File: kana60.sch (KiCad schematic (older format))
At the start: 2 parts

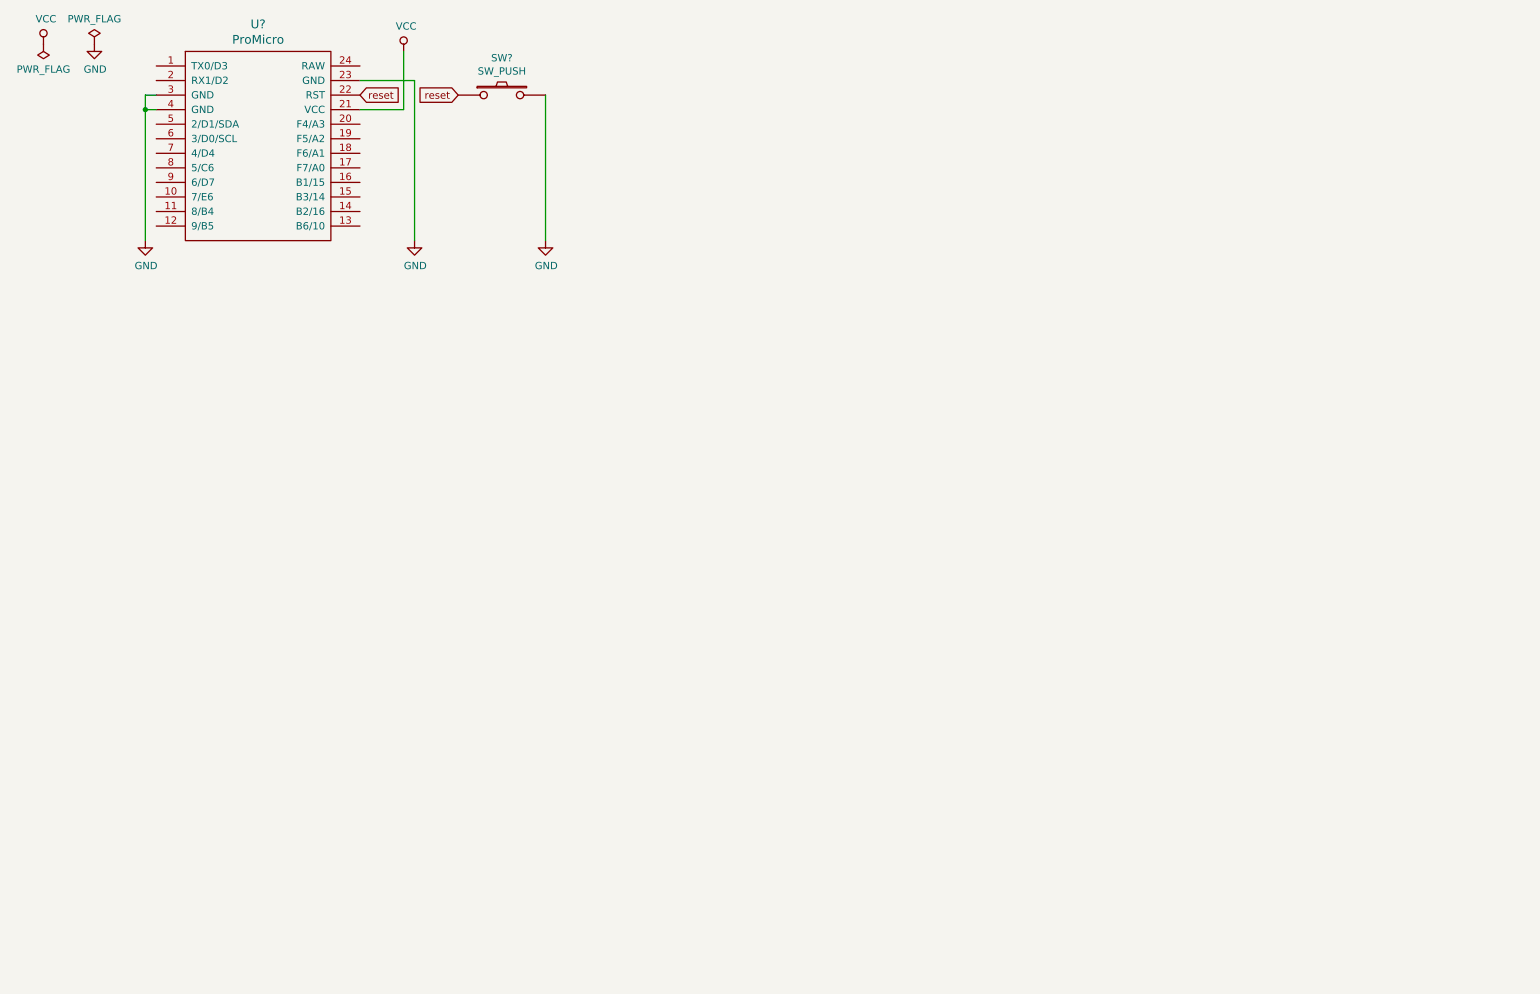
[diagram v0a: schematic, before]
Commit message: add key switches
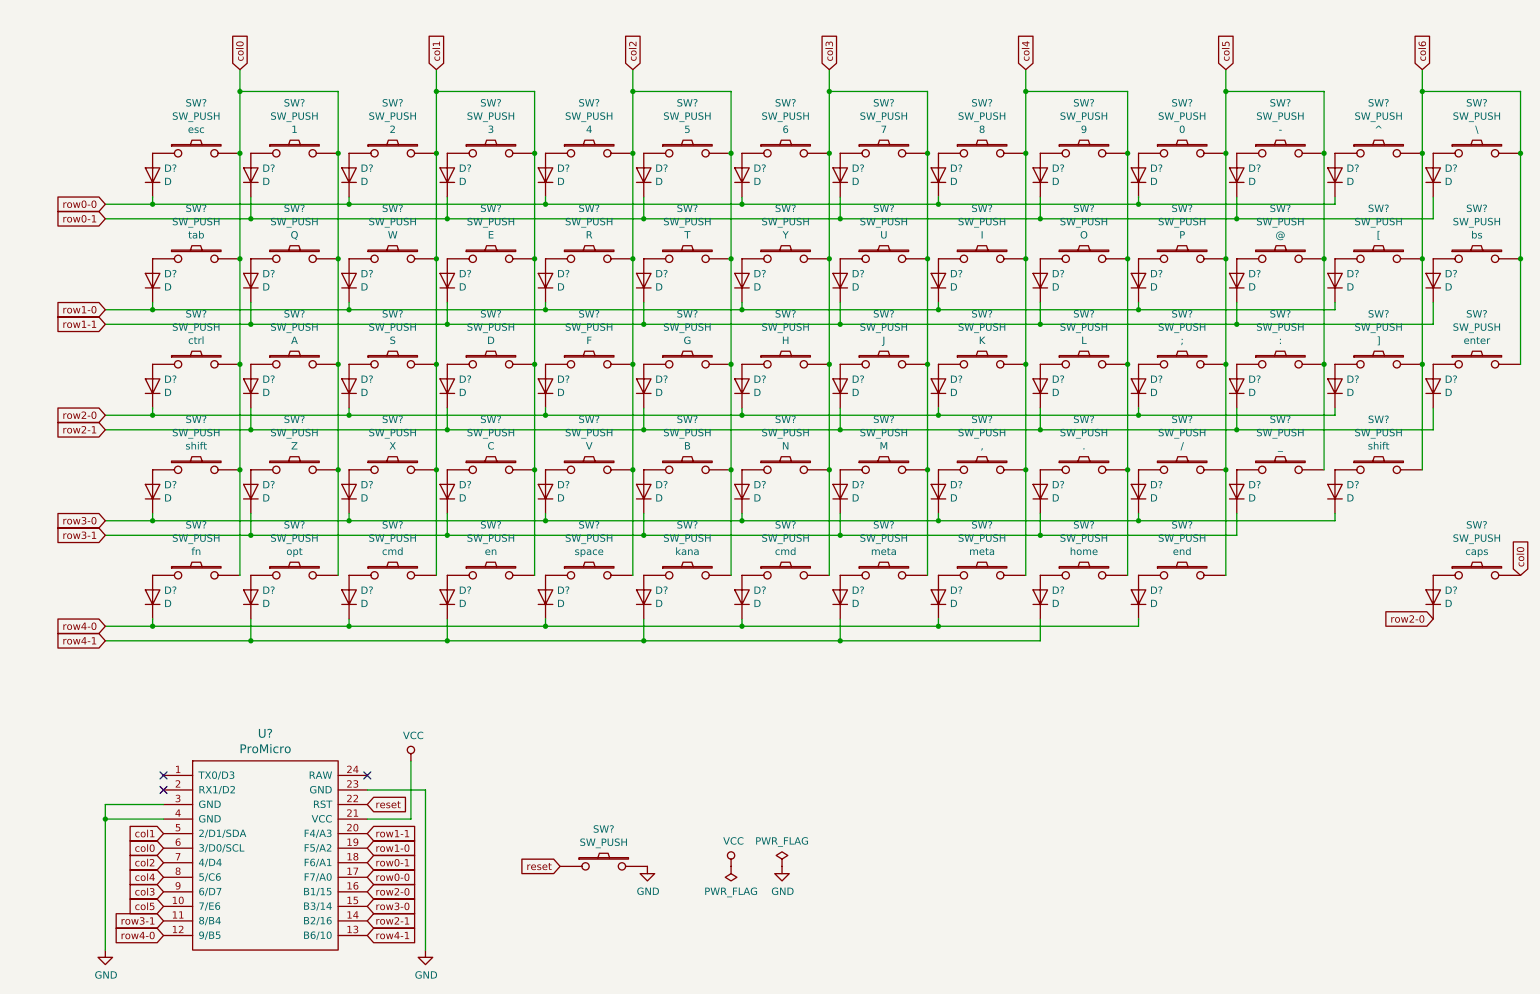
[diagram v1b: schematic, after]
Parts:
- added D? (x67): D, symbol Device:D
- added SW?: SW_PUSH, esc, symbol kbd:SW_PUSH
- added SW?: SW_PUSH, tab, symbol kbd:SW_PUSH
- added SW?: SW_PUSH, 1, symbol kbd:SW_PUSH
- added SW?: SW_PUSH, Q, symbol kbd:SW_PUSH
- added SW?: SW_PUSH, ctrl, symbol kbd:SW_PUSH
- added SW? (x2): SW_PUSH, shift, symbol kbd:SW_PUSH
- added SW?: SW_PUSH, A, symbol kbd:SW_PUSH
- added SW?: SW_PUSH, Z, symbol kbd:SW_PUSH
- added SW?: SW_PUSH, fn, symbol kbd:SW_PUSH
- added SW?: SW_PUSH, opt, symbol kbd:SW_PUSH
- added SW?: SW_PUSH, 2, symbol kbd:SW_PUSH
- added SW?: SW_PUSH, W, symbol kbd:SW_PUSH
- added SW?: SW_PUSH, 3, symbol kbd:SW_PUSH
- added SW?: SW_PUSH, E, symbol kbd:SW_PUSH
- added SW?: SW_PUSH, S, symbol kbd:SW_PUSH
- added SW?: SW_PUSH, X, symbol kbd:SW_PUSH
- added SW?: SW_PUSH, D, symbol kbd:SW_PUSH
- added SW?: SW_PUSH, C, symbol kbd:SW_PUSH
- added SW? (x2): SW_PUSH, cmd, symbol kbd:SW_PUSH
- added SW?: SW_PUSH, en, symbol kbd:SW_PUSH
- added SW?: SW_PUSH, 4, symbol kbd:SW_PUSH
- added SW?: SW_PUSH, R, symbol kbd:SW_PUSH
- added SW?: SW_PUSH, 5, symbol kbd:SW_PUSH
- added SW?: SW_PUSH, T, symbol kbd:SW_PUSH
- added SW?: SW_PUSH, F, symbol kbd:SW_PUSH
- added SW?: SW_PUSH, V, symbol kbd:SW_PUSH
- added SW?: SW_PUSH, G, symbol kbd:SW_PUSH
- added SW?: SW_PUSH, B, symbol kbd:SW_PUSH
- added SW?: SW_PUSH, space, symbol kbd:SW_PUSH
- added SW?: SW_PUSH, 6, symbol kbd:SW_PUSH
- added SW?: SW_PUSH, Y, symbol kbd:SW_PUSH
- added SW?: SW_PUSH, 7, symbol kbd:SW_PUSH
- added SW?: SW_PUSH, H, symbol kbd:SW_PUSH
- added SW?: SW_PUSH, N, symbol kbd:SW_PUSH
- added SW?: SW_PUSH, 8, symbol kbd:SW_PUSH
- added SW?: SW_PUSH, U, symbol kbd:SW_PUSH
- added SW?: SW_PUSH, 9, symbol kbd:SW_PUSH
- added SW?: SW_PUSH, I, symbol kbd:SW_PUSH
- added SW?: SW_PUSH, J, symbol kbd:SW_PUSH
- added SW?: SW_PUSH, M, symbol kbd:SW_PUSH
- added SW?: SW_PUSH, K, symbol kbd:SW_PUSH
- added SW?: SW_PUSH, ,, symbol kbd:SW_PUSH
- added SW?: SW_PUSH, kana, symbol kbd:SW_PUSH
- added SW?: SW_PUSH, 0, symbol kbd:SW_PUSH
- added SW?: SW_PUSH, O, symbol kbd:SW_PUSH
- added SW?: SW_PUSH, -, symbol kbd:SW_PUSH
- added SW?: SW_PUSH, P, symbol kbd:SW_PUSH
- added SW?: SW_PUSH, L, symbol kbd:SW_PUSH
- added SW?: SW_PUSH, ., symbol kbd:SW_PUSH
- added SW?: SW_PUSH, ;, symbol kbd:SW_PUSH
- added SW?: SW_PUSH, /, symbol kbd:SW_PUSH
- added SW? (x2): SW_PUSH, meta, symbol kbd:SW_PUSH
- added SW?: SW_PUSH, ^, symbol kbd:SW_PUSH
- added SW?: SW_PUSH, @, symbol kbd:SW_PUSH
- added SW?: SW_PUSH, \\, symbol kbd:SW_PUSH
- added SW?: SW_PUSH, [, symbol kbd:SW_PUSH
- added SW?: SW_PUSH, :, symbol kbd:SW_PUSH
- added SW?: SW_PUSH, _, symbol kbd:SW_PUSH
- added SW?: SW_PUSH, ], symbol kbd:SW_PUSH
- added SW?: SW_PUSH, home, symbol kbd:SW_PUSH
- added SW?: SW_PUSH, end, symbol kbd:SW_PUSH
- added SW?: SW_PUSH, bs, symbol kbd:SW_PUSH
- added SW?: SW_PUSH, enter, symbol kbd:SW_PUSH
- added SW?: SW_PUSH, caps, symbol kbd:SW_PUSH
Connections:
- net col5: now reaches U?.10 (7/E6)
- net col5: now also SW?.2, SW?.2, SW?.2, SW?.2, SW?.2, SW?.2, SW?.2, SW?.2, SW?.2
- net row3-1: now reaches U?.11 (8/B4)
- net row3-1: now also D?.1 (K), D?.1 (K), D?.1 (K), D?.1 (K), D?.1 (K), D?.1 (K)
- net row4-0: now reaches U?.12 (9/B5)
- net row4-0: now also D?.1 (K), D?.1 (K), D?.1 (K), D?.1 (K), D?.1 (K), D?.1 (K)
- net row4-1: now reaches U?.13 (B6/10)
- net row4-1: now also D?.1 (K), D?.1 (K), D?.1 (K), D?.1 (K), D?.1 (K)
- net row2-1: now reaches U?.14 (B2/16)
- net row2-1: now also D?.1 (K), D?.1 (K), D?.1 (K), D?.1 (K), D?.1 (K), D?.1 (K), D?.1 (K)
- net row3-0: now reaches U?.15 (B3/14)
- net row3-0: now also D?.1 (K), D?.1 (K), D?.1 (K), D?.1 (K), D?.1 (K), D?.1 (K), D?.1 (K)
- net row2-0: now reaches U?.16 (B1/15)
- net row2-0: now also D?.1 (K), D?.1 (K), D?.1 (K), D?.1 (K), D?.1 (K), D?.1 (K), D?.1 (K), D?.1 (K)
- net row0-0: now reaches U?.17 (F7/A0)
- net row0-0: now also D?.1 (K), D?.1 (K), D?.1 (K), D?.1 (K), D?.1 (K), D?.1 (K), D?.1 (K)
- net row0-1: now reaches U?.18 (F6/A1)
- net row0-1: now also D?.1 (K), D?.1 (K), D?.1 (K), D?.1 (K), D?.1 (K), D?.1 (K), D?.1 (K)
- net row1-0: now reaches U?.19 (F5/A2)
- net row1-0: now also D?.1 (K), D?.1 (K), D?.1 (K), D?.1 (K), D?.1 (K), D?.1 (K), D?.1 (K)
- net row1-1: now reaches U?.20 (F4/A3)
- net row1-1: now also D?.1 (K), D?.1 (K), D?.1 (K), D?.1 (K), D?.1 (K), D?.1 (K), D?.1 (K)
- net col1: now reaches U?.5 (2/D1/SDA)
- net col1: now also SW?.2, SW?.2, SW?.2, SW?.2, SW?.2, SW?.2, SW?.2, SW?.2, SW?.2, SW?.2
- net col0: now reaches U?.6 (3/D0/SCL)
- net col0: now also SW?.2, SW?.2, SW?.2, SW?.2, SW?.2, SW?.2, SW?.2, SW?.2, SW?.2, SW?.2, SW?.2
- net col2: now reaches U?.7 (4/D4)
- net col2: now also SW?.2, SW?.2, SW?.2, SW?.2, SW?.2, SW?.2, SW?.2, SW?.2, SW?.2, SW?.2
- net col4: now reaches U?.8 (5/C6)
- net col4: now also SW?.2, SW?.2, SW?.2, SW?.2, SW?.2, SW?.2, SW?.2, SW?.2, SW?.2, SW?.2
- net col3: now reaches U?.9 (6/D7)
- net col3: now also SW?.2, SW?.2, SW?.2, SW?.2, SW?.2, SW?.2, SW?.2, SW?.2, SW?.2, SW?.2
- new net: D?.2 (A), SW?.1 (x67)
- new net col6: SW?.2, SW?.2, SW?.2, SW?.2, SW?.2, SW?.2, SW?.2
- no-connect marks 0 -> 3
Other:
- moved on the sheet: SW?, U?

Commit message: annotation and rule check
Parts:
- gave numbers to parts that had none: 136
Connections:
- net col2: now also U1.2 (RX1/D2); no longer U1.7 (4/D4)
- net col3: now also U1.7 (4/D4); no longer U1.9 (6/D7)
- net col4: now also U1.9 (6/D7); no longer U1.8 (5/C6)
- net col5: now also U1.8 (5/C6); no longer U1.10 (7/E6)
- net col6: now also U1.10 (7/E6)
- no-connect marks 3 -> 2

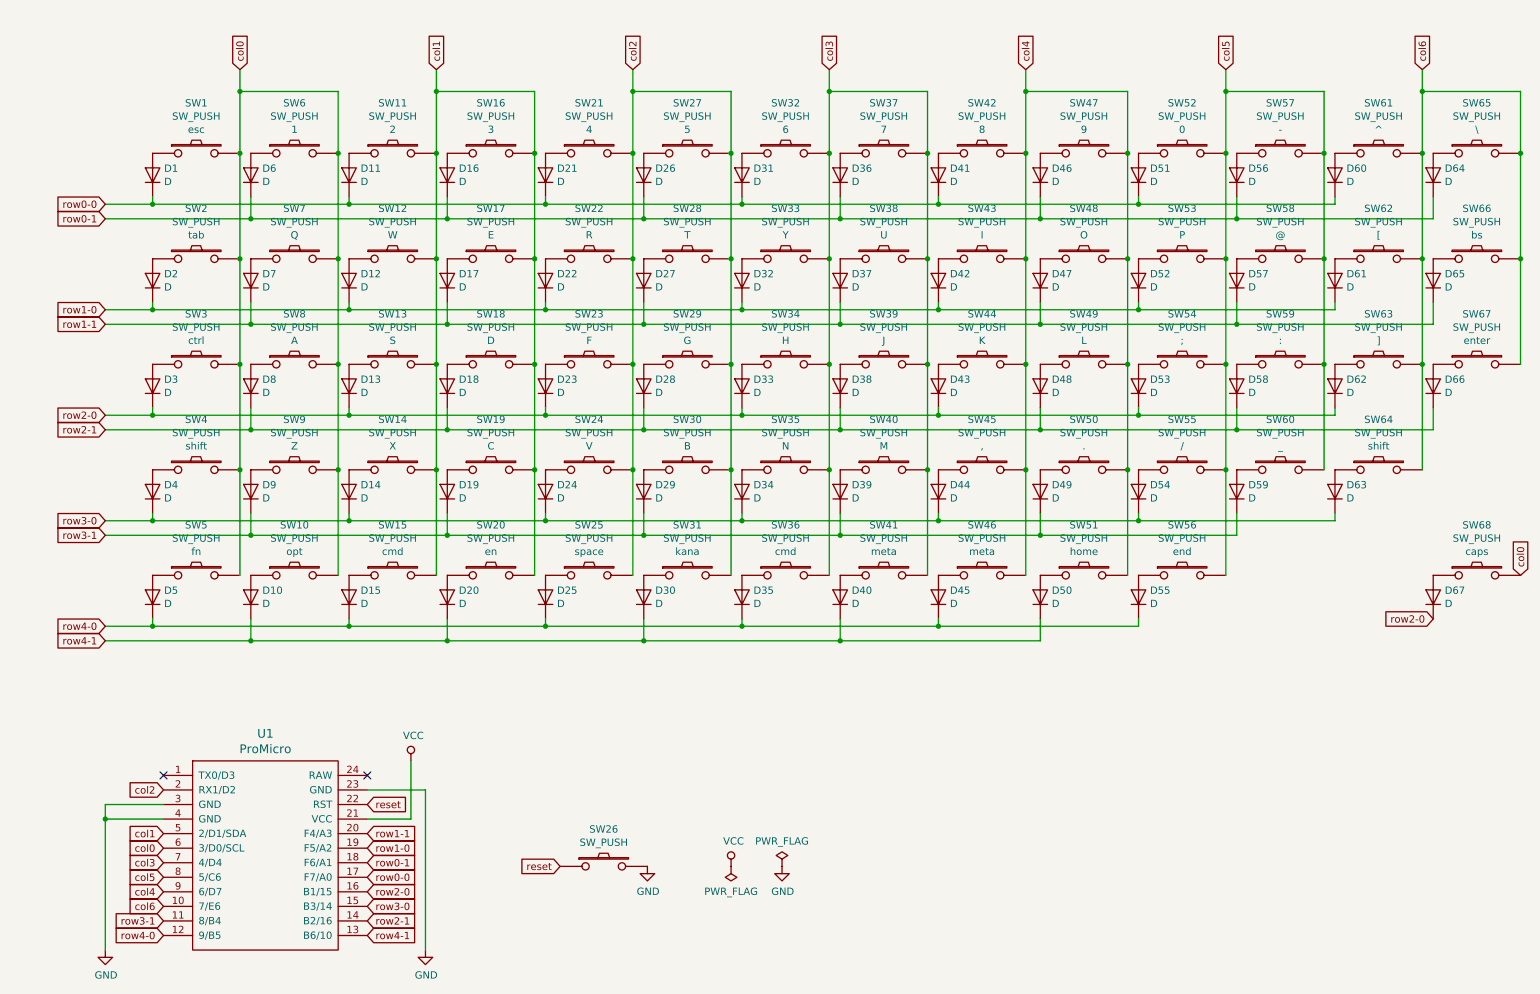
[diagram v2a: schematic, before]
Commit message: fix footprint
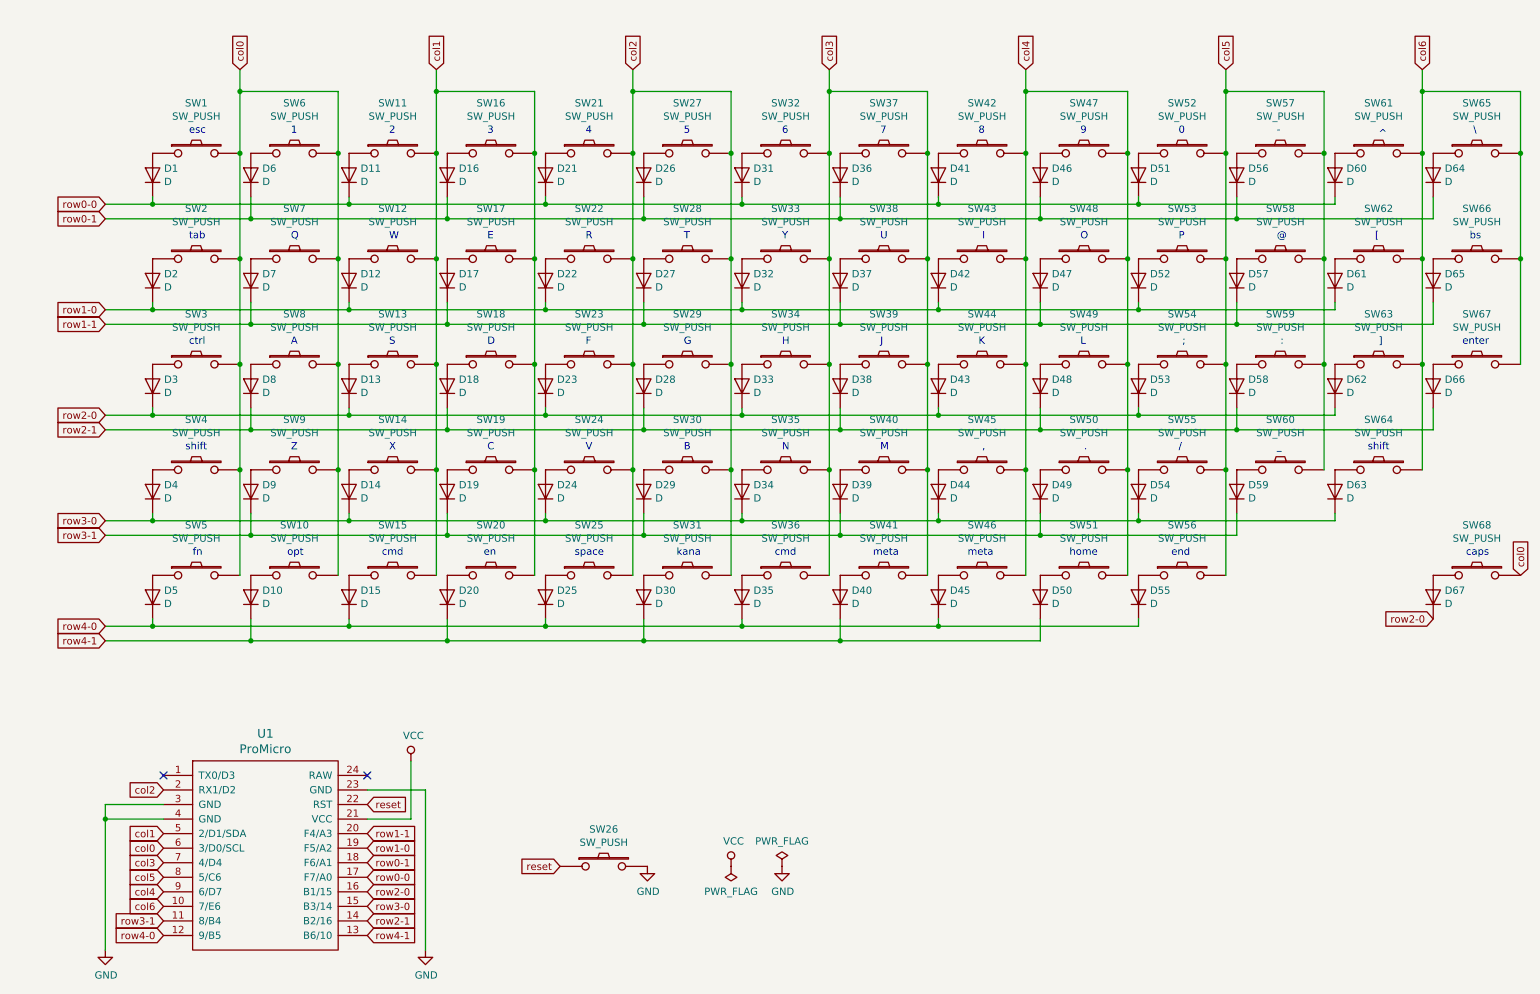
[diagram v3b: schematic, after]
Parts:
- SW1: footprint esc -> (none)
- SW10: footprint opt -> (none)
- SW11: footprint 2 -> (none)
- SW12: footprint W -> (none)
- SW13: footprint S -> (none)
- SW14: footprint X -> (none)
- SW15, SW36: footprint cmd -> (none)
- SW16: footprint 3 -> (none)
- SW17: footprint E -> (none)
- SW18: footprint D -> (none)
- SW19: footprint C -> (none)
- SW2: footprint tab -> (none)
- SW20: footprint en -> (none)
- SW21: footprint 4 -> (none)
- SW22: footprint R -> (none)
- SW23: footprint F -> (none)
- SW24: footprint V -> (none)
- SW25: footprint space -> (none)
- SW27: footprint 5 -> (none)
- SW28: footprint T -> (none)
- SW29: footprint G -> (none)
- SW3: footprint ctrl -> (none)
- SW30: footprint B -> (none)
- SW31: footprint kana -> (none)
- SW32: footprint 6 -> (none)
- SW33: footprint Y -> (none)
- SW34: footprint H -> (none)
- SW35: footprint N -> (none)
- SW37: footprint 7 -> (none)
- SW38: footprint U -> (none)
- SW39: footprint J -> (none)
- SW4, SW64: footprint shift -> (none)
- SW40: footprint M -> (none)
- SW41, SW46: footprint meta -> (none)
- SW42: footprint 8 -> (none)
- SW43: footprint I -> (none)
- SW44: footprint K -> (none)
- SW45: footprint , -> (none)
- SW47: footprint 9 -> (none)
- SW48: footprint O -> (none)
- SW49: footprint L -> (none)
- SW5: footprint fn -> (none)
- SW50: footprint . -> (none)
- SW51: footprint home -> (none)
- SW52: footprint 0 -> (none)
- SW53: footprint P -> (none)
- SW54: footprint ; -> (none)
- SW55: footprint / -> (none)
- SW56: footprint end -> (none)
- SW57: footprint - -> (none)
- SW58: footprint @ -> (none)
- SW59: footprint : -> (none)
- SW6: footprint 1 -> (none)
- SW60: footprint _ -> (none)
- SW61: footprint ^ -> (none)
- SW62: footprint [ -> (none)
- SW63: footprint ] -> (none)
- SW65: footprint \\ -> (none)
- SW66: footprint bs -> (none)
- SW67: footprint enter -> (none)
- SW68: footprint caps -> (none)
- SW7: footprint Q -> (none)
- SW8: footprint A -> (none)
- SW9: footprint Z -> (none)
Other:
- note added: ","
- note added: "-"
- note added: "."
- note added: "/"
- note added: "0"
- note added: "1"
- note added: "2"
- note added: "3"
- note added: "4"
- note added: "5"
- note added: "6"
- note added: "7"
- note added: "8"
- note added: "9"
- note added: ":"
- note added: ";"
- note added: "@"
- note added: "A"
- note added: "B"
- note added: "C"
- note added: "D"
- note added: "E"
- note added: "F"
- note added: "G"
- note added: "H"
- note added: "I"
- note added: "J"
- note added: "K"
- note added: "L"
- note added: "M"
- note added: "N"
- note added: "O"
- note added: "P"
- note added: "Q"
- note added: "R"
- note added: "S"
- note added: "T"
- note added: "U"
- note added: "V"
- note added: "W"
- note added: "X"
- note added: "Y"
- note added: "Z"
- note added: "["
- note added: "\"
- note added: "]"
- note added: "^"
- note added: "_"
- note added: "bs"
- note added: "caps"
- note added: "cmd"
- note added: "ctrl"
- note added: "en"
- note added: "end"
- note added: "enter"
- note added: "esc"
- note added: "fn"
- note added: "home"
- note added: "kana"
- note added: "meta"
- note added: "opt"
- note added: "shift"
- note added: "space"
- note added: "tab"

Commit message: add PCB footprint
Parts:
- D1, D10, D11, D12, D13, D14, D15, D16, D17, D18, D19, D2, D20, D21, D22, D23, D24, D25, D26, D27, D28, D29, D3, D30, D31, D32, D33, D34, D35, D36, D37, D38, D39, D4, D40, D41, D42, D43, D44, D45, D46, D47, D48, D49, D5, D50, D51, D52, D53, D54, D55, D56, D57, D58, D59, D6, D60, D61, D62, D63, D64, D65, D66, D67, D7, D8, D9: footprint (none) -> kbd:D3_TH_SMD
- SW1, SW10, SW11, SW12, SW13, SW14, SW15, SW16, SW17, SW18, SW19, SW2, SW20, SW21, SW22, SW23, SW24, SW25, SW27, SW28, SW29, SW3, SW30, SW31, SW32, SW33, SW34, SW35, SW36, SW37, SW38, SW39, SW4, SW40, SW41, SW42, SW43, SW44, SW45, SW46, SW47, SW48, SW49, SW5, SW50, SW51, SW52, SW53, SW54, SW55, SW56, SW57, SW58, SW59, SW6, SW60, SW61, SW62, SW63, SW64, SW65, SW66, SW67, SW68, SW7, SW8, SW9: footprint (none) -> kbd:CherryMX_Choc_1u
- SW26: footprint (none) -> kbd:ResetSW_1side
- U1: footprint (none) -> Keebio-Parts:ArduinoProMicro

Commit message: update label
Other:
- note added: "down"
- note added: "left"
- note added: "right"
- note added: "up"
- note removed: "end"
- note removed: "home"
- note removed: "meta"
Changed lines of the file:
@@
 cmd
 Text Notes 6400 4250 0    50   ~ 0
-meta
+left
 Text Notes 7050 4250 0    50   ~ 0
-meta
-Text Notes 7750 4250 0    50   ~ 0
-home
+down
+Text Notes 7800 4250 0    50   ~ 0
+up
 Text Notes 8450 4250 0    50   ~ 0
-end
+right
 Text Notes 10475 4250 0    50   ~ 0
 caps

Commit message: reannotate
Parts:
- renumbered D46 to D10, D51 to D11, D56 to D12, D60 to D13, D64 to D14, D2 to D15, D7 to D16, D12 to D17, D17 to D18, D22 to D19, D6 to D2, D27 to D20, D32 to D21, D37 to D22, D42 to D23, D47 to D24, D52 to D25, D57 to D26, D61 to D27, D65 to D28, D3 to D29, D11 to D3, D8 to D30, D13 to D31, D18 to D32, D23 to D33, D28 to D34, D33 to D35, D38 to D36, D43 to D37, D48 to D38, D53 to D39, D16 to D4, D58 to D40, D62 to D41, D66 to D42, D4 to D43, D9 to D44, D14 to D45, D19 to D46, D24 to D47, D29 to D48, D34 to D49, D21 to D5, D39 to D50, D44 to D51, D49 to D52, D54 to D53, D59 to D54, D63 to D55, D5 to D56, D10 to D57, D15 to D58, D20 to D59, D26 to D6, D25 to D60, D30 to D61, D35 to D62, D40 to D63, D45 to D64, D50 to D65, D55 to D66, D31 to D7, D36 to D8, D41 to D9, SW47 to SW10, SW52 to SW11, SW57 to SW12, SW61 to SW13, SW65 to SW14, SW2 to SW15, SW7 to SW16, SW12 to SW17, SW17 to SW18, SW22 to SW19, SW6 to SW2, SW28 to SW20, SW33 to SW21, SW38 to SW22, SW43 to SW23, SW48 to SW24, SW53 to SW25, SW58 to SW26, SW62 to SW27, SW66 to SW28, SW3 to SW29, SW11 to SW3, SW8 to SW30, SW13 to SW31, SW18 to SW32, SW23 to SW33, SW29 to SW34, SW34 to SW35, SW39 to SW36, SW44 to SW37, SW49 to SW38, SW54 to SW39, SW16 to SW4, SW59 to SW40, SW63 to SW41, SW67 to SW42, SW4 to SW43, SW9 to SW44, SW14 to SW45, SW19 to SW46, SW24 to SW47, SW30 to SW48, SW35 to SW49, SW21 to SW5, SW40 to SW50, SW45 to SW51, SW50 to SW52, SW55 to SW53, SW60 to SW54, SW64 to SW55, SW5 to SW56, SW10 to SW57, SW15 to SW58, SW20 to SW59, SW27 to SW6, SW25 to SW60, SW31 to SW61, SW36 to SW62, SW41 to SW63, SW46 to SW64, SW51 to SW65, SW56 to SW66, SW68 to SW67, SW26 to SW68, SW32 to SW7, SW37 to SW8, SW42 to SW9
